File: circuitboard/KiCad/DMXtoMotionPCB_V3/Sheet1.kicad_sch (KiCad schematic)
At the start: 51 parts, among them J1 12V In, J10 D2, J2 XLR3 IN, J3 XLR3 OUT, J4 D1, J5 INTERFACE, J6 A0, J7 A1, J8 D0, J9 D3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

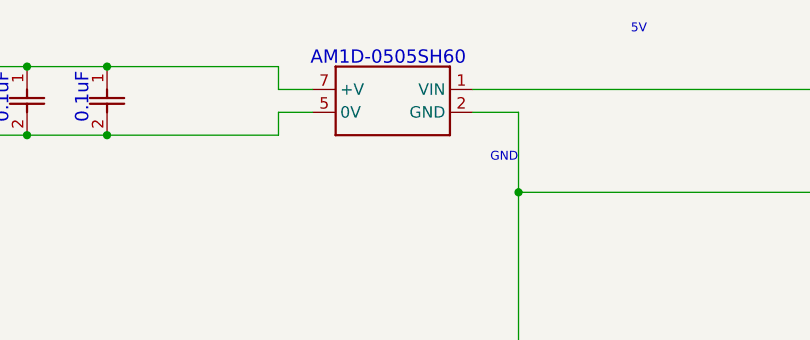
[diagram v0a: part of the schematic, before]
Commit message: Slight modifications on KiCAD V3 files. Generated fabrication files
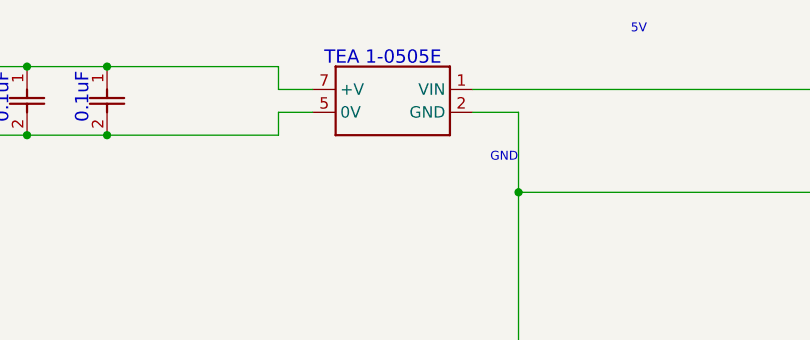
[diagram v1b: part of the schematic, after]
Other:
- note added: "TEA 1-0505E"
- note removed: "AM1D-0505SH60"
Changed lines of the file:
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@@
 		)
 	)
-	(text "AM1D-0505SH60"
+	(text "TEA 1-0505E"
 		(exclude_from_sim no)
-		(at 195.319 24.13 0)
+		(at 196.85 24.13 0)
 		(effects
 			(font

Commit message: KiCAD files
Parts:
- U4: value L78S05CV -> LM78M05CT
- VO2, VO3: value 6N137M_10 -> 6N137M
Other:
- note added: "LM78M05CT"
- note removed: "" ""
- note removed: "L78S05CV"
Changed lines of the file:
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@@
 		)
 	)
-	(text "\" \""
+	(text "6N137M"
 		(exclude_from_sim no)
-		(at 160.274 113.538 0)
+		(at 157.988 113.792 0)
 		(effects
 			(font
@@
 		)
 	)
-	(text "L78S05CV"
+	(text "LM78M05CT"
 		(exclude_from_sim no)
 		(at 263.475 21.59 0)
@@
 			)
 		)
-		(property "Value" "L78S05CV"
+		(property "Value" "LM78M05CT"
 			(at 269.24 26.67 0)
 			(effects
@@
 			)
 		)
-		(property "Value" "6N137M_10"
+		(property "Value" "6N137M"
 			(at 162.56 120.65 0)
 			(effects
@@
 			)
 		)
-		(property "Value" "6N137M_10"
+		(property "Value" "6N137M"
 			(at 162.56 140.97 0)
 			(effects
